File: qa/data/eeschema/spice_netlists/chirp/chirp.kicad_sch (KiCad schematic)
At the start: 2 parts

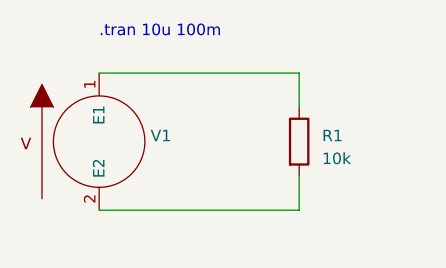
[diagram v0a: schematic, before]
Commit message: Generate .save all and .probe alli in Spice exporter
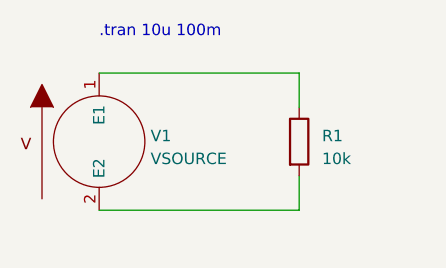
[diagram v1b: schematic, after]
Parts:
- V1: value (none) -> VSOURCE
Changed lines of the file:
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@@
       (effects (font (size 1.27 1.27)) (justify left))
     )
-    (property "Value" "" (id 1) (at 166.37 116.84 0)
+    (property "Value" "VSOURCE" (id 1) (at 166.37 116.84 0)
       (effects (font (size 1.27 1.27)) (justify left))
     )

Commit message: Make sim QA tests compare result vectors, not netlist text
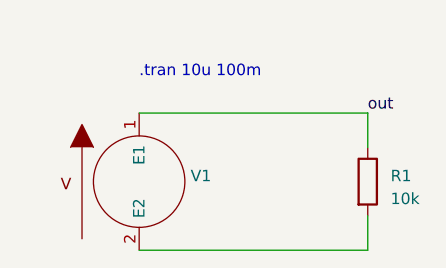
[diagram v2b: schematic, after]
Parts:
- V1: value VSOURCE -> (none); Model_Library chirp.lib -> chirp.lib.spice
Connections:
- net out: now reaches R1.1, V1.1 (E1)
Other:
- moved on the sheet: R1, V1
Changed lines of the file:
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@@
 (kicad_sch (version 20220331) (generator eeschema)
   (paper "A4")
-  (wire (pts (xy 182.88 107.315) (xy 182.88 111.125))
+  (wire (pts (xy 190.5 111.76) (xy 190.5 115.57))
     (stroke (width 0) (type default))
   )
-  (wire (pts (xy 160.655 122.555) (xy 182.88 122.555))
+  (wire (pts (xy 165.1 127) (xy 190.5 127))
     (stroke (width 0) (type default))
   )
-  (wire (pts (xy 160.655 107.315) (xy 182.88 107.315))
+  (wire (pts (xy 165.1 111.76) (xy 190.5 111.76))
     (stroke (width 0) (type default))
   )
-  (wire (pts (xy 182.88 122.555) (xy 182.88 118.745))
+  (wire (pts (xy 190.5 127) (xy 190.5 123.19))
     (stroke (width 0) (type default))
   )
-  (text ".tran 10u 100m" (at 160.655 103.505 0)
+  (text ".tran 10u 100m" (at 165.1 107.95 0)
     (effects (font (size 1.27 1.27)) (justify left bottom))
   )
-  (symbol (lib_id "pspice:VSOURCE") (at 160.655 114.935 0) (unit 1)
+  (label "out" (at 190.5 111.76 0) (fields_autoplaced)
+    (effects (font (size 1.27 1.27)) (justify left bottom))
+  )
+  (symbol (lib_id "pspice:VSOURCE") (at 165.1 119.38 0) (unit 1)
     (in_bom yes) (on_board yes) (fields_autoplaced)
-    (property "Reference" "V1" (id 0) (at 166.37 114.3 0)
+    (property "Reference" "V1" (id 0) (at 170.815 118.745 0)
       (effects (font (size 1.27 1.27)) (justify left))
     )
-    (property "Value" "VSOURCE" (id 1) (at 166.37 116.84 0)
+    (property "Value" "" (id 1) (at 170.815 121.285 0)
       (effects (font (size 1.27 1.27)) (justify left))
     )
-    (property "Footprint" "" (id 2) (at 160.655 114.935 0)
+    (property "Footprint" "" (id 2) (at 165.1 119.38 0)
       (effects (font (size 1.27 1.27)) hide)
     )
-    (property "Datasheet" "~" (id 3) (at 160.655 114.935 0)
+    (property "Datasheet" "~" (id 3) (at 165.1 119.38 0)
       (effects (font (size 1.27 1.27)) hide)
     )
-    (property "Model_Name" "chirp" (id 4) (at 160.655 114.935 0)
+    (property "Model_Name" "chirp" (id 4) (at 165.1 119.38 0)
       (effects (font (size 1.27 1.27)) hide)
     )
-    (property "Model_Library" "chirp.lib" (id 5) (at 160.655 114.935 0)
+    (property "Model_Library" "chirp.lib.spice" (id 5) (at 165.1 119.38 0)
       (effects (font (size 1.27 1.27)) hide)
     )
-    (property "Model_Device" "SUBCKT" (id 6) (at 160.655 114.935 0)
+    (property "Model_Device" "SUBCKT" (id 6) (at 165.1 119.38 0)
       (effects (font (size 1.27 1.27)) hide)
     )
-    (property "Model_Params" "bf=1k ef=3k bt=30m et=70m" (id 7) (at 160.655 114.935 0)
+    (property "Model_Params" "bf=1k ef=3k bt=30m et=70m" (id 7) (at 165.1 119.38 0)
       (effects (font (size 1.27 1.27)) hide)
     )
-    (property "Model_Pins" "1 2" (id 8) (at 160.655 114.935 0)
+    (property "Model_Pins" "1 2" (id 8) (at 165.1 119.38 0)
       (effects (font (size 1.27 1.27)) hide)
     )
@@
     (pin "2")
   )
-  (symbol (lib_id "Device:R") (at 182.88 114.935 0) (unit 1)
+  (symbol (lib_id "Device:R") (at 190.5 119.38 0) (unit 1)
     (in_bom yes) (on_board yes) (fields_autoplaced)
-    (property "Reference" "R1" (id 0) (at 185.42 114.3 0)
+    (property "Reference" "R1" (id 0) (at 193.04 118.745 0)
       (effects (font (size 1.27 1.27)) (justify left))
     )
-    (property "Value" "10k" (id 1) (at 185.42 116.84 0)
+    (property "Value" "10k" (id 1) (at 193.04 121.285 0)
       (effects (font (size 1.27 1.27)) (justify left))
     )
-    (property "Footprint" "" (id 2) (at 181.102 114.935 90)
+    (property "Footprint" "" (id 2) (at 188.722 119.38 90)
       (effects (font (size 1.27 1.27)) hide)
     )
-    (property "Datasheet" "~" (id 3) (at 182.88 114.935 0)
+    (property "Datasheet" "~" (id 3) (at 190.5 119.38 0)
       (effects (font (size 1.27 1.27)) hide)
     )
